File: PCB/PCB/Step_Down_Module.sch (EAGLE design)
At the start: 4 parts, among them Q1 TPH2900ENH

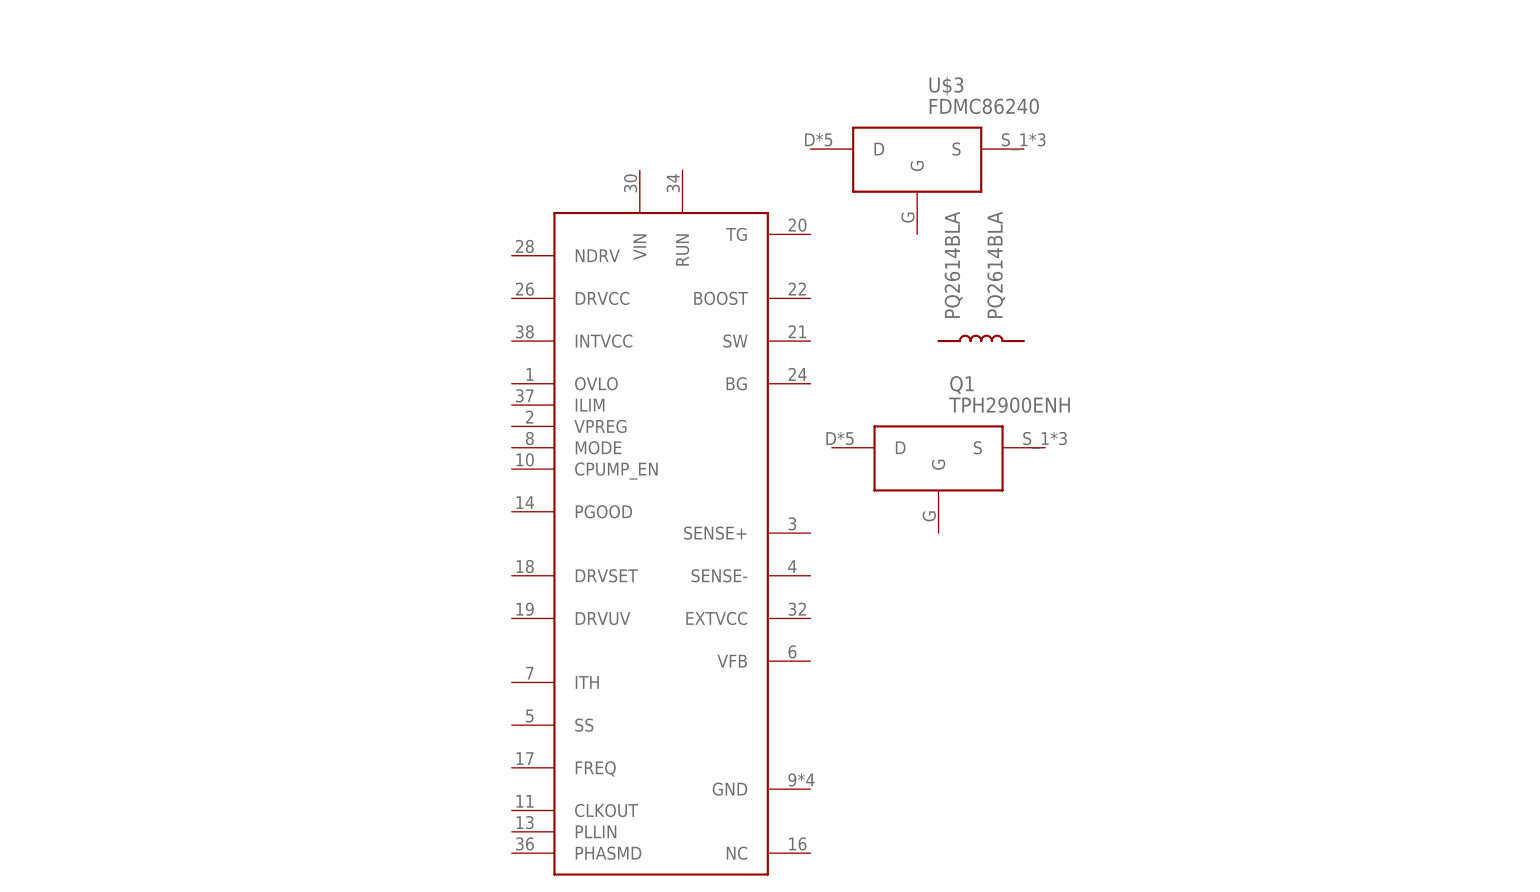
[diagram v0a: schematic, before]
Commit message: Working on schematic, slightly updated mosfets
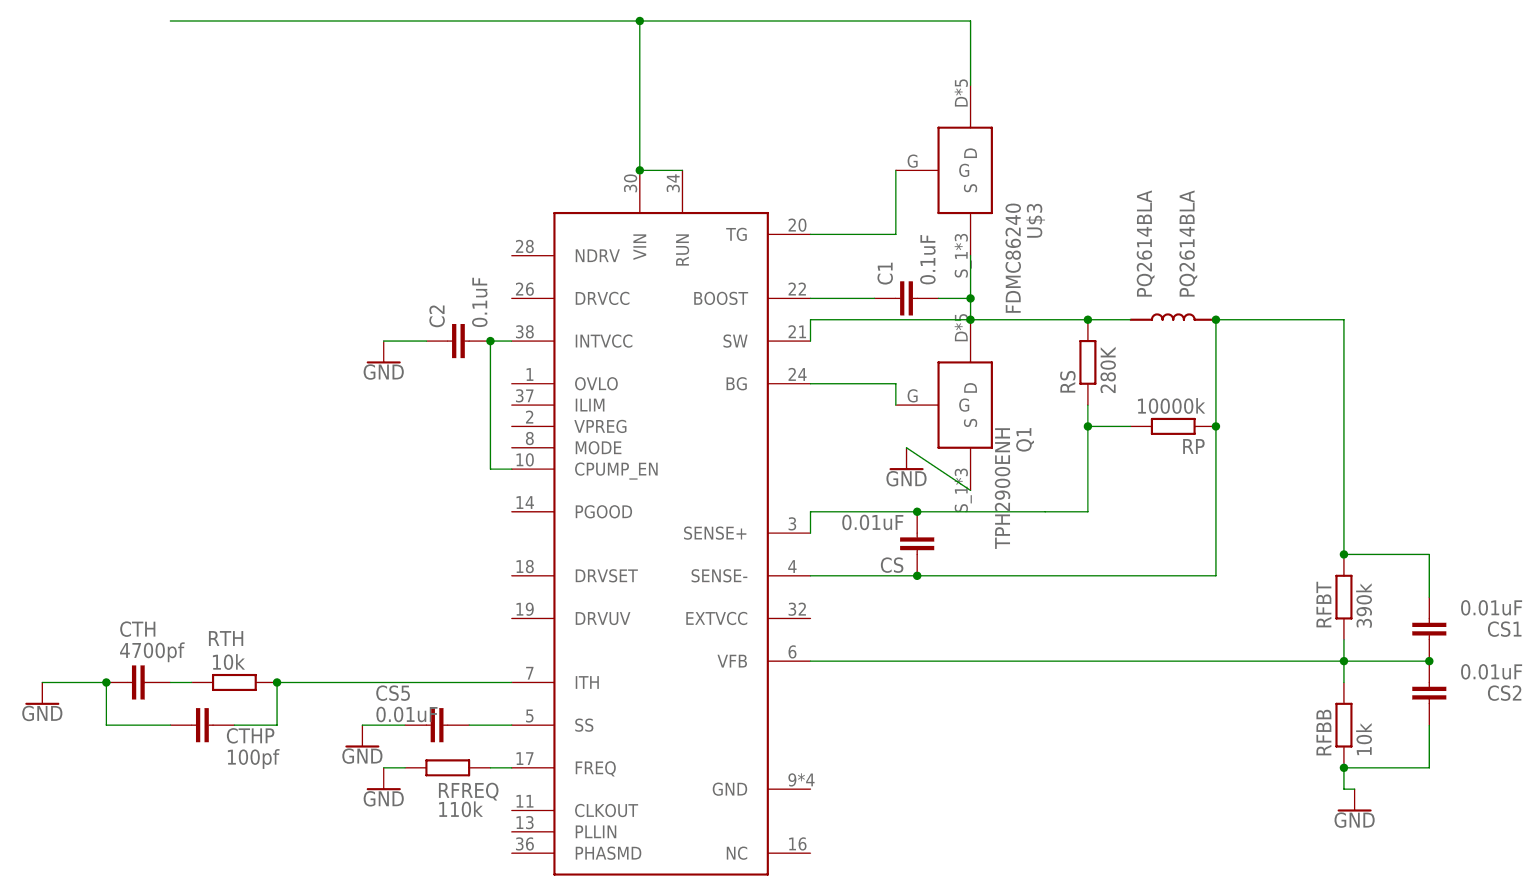
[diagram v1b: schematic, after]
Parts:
- added C1, C2: 0.1uF, rcl:C-EUC0805
- added CS, CS1, CS2, CS5: 0.01uF, rcl:C-EUC0805
- added CTH: 4700pf, rcl:C-EUC0805
- added CTHP: 100pf, rcl:C-EUC0805
- added RFBB, RTH: 10k, rcl:R-EU_R0805
- added RFBT: 390k, rcl:R-EU_R0805
- added RFREQ: 110k, rcl:R-EU_R0805
- added RP: 10000k, rcl:R-EU_R0805
- added RS: 280K, rcl:R-EU_R0805
- Q1: SPICEPREFIX (none) -> Q
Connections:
- new net GND: C2.1, CS2.1, CS5.2, CTH.2, CTHP.2, Q1.S, RFBB.1, RFREQ.1
- new net N$1: U$1.TG, U$3.G
- new net N$10: CTHP.1, RTH.1, U$1.ITH
- new net N$11: RFREQ.2, U$1.FREQ
- new net N$12: CTH.1, RTH.2
- new net N$13: C2.2, U$1.CPUMP_EN, U$1.INTVCC
- new net N$2: Q1.G, U$1.BG
- new net N$3: C1.2, Q1.D, RS.2, U$1.SW, U$2.P$1, U$3.S
- new net N$4: C1.1, U$1.BOOST
- new net N$5: CS.1, CS1.2, RFBT.2, RP.1, U$1.SENSE-, U$2.P$2
- new net N$6: CS.2, RP.2, RS.1, U$1.SENSE+
- new net N$7: CS5.1, U$1.SS
- new net N$8: CS1.1, CS2.2, RFBB.2, RFBT.1, U$1.VFB
- new net N$9: U$1.RUN, U$1.VIN, U$3.D
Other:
- moved on the sheet: Q1, U$3

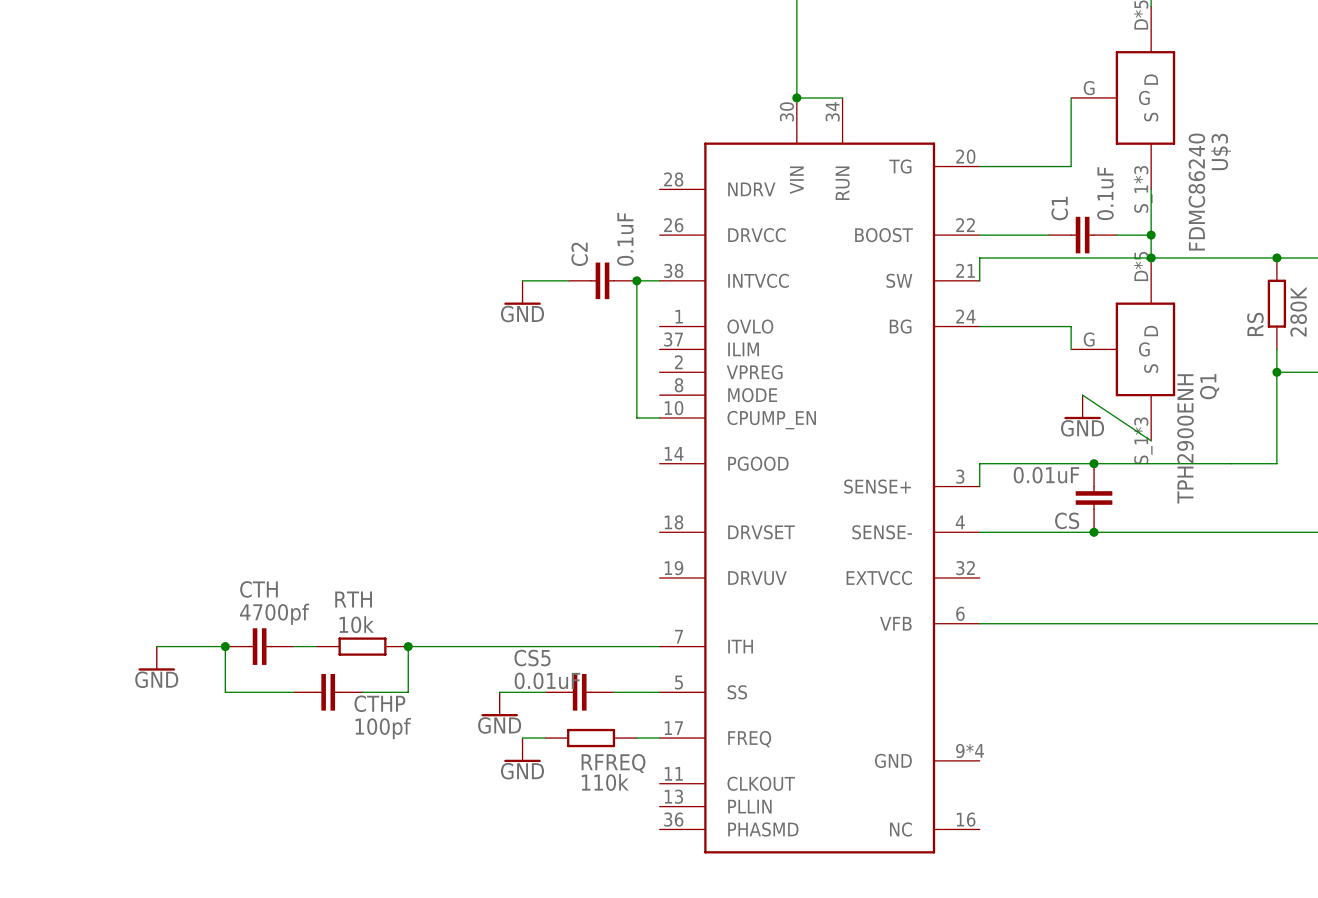
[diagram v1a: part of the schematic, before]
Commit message: Working on schematic - functions of other pins
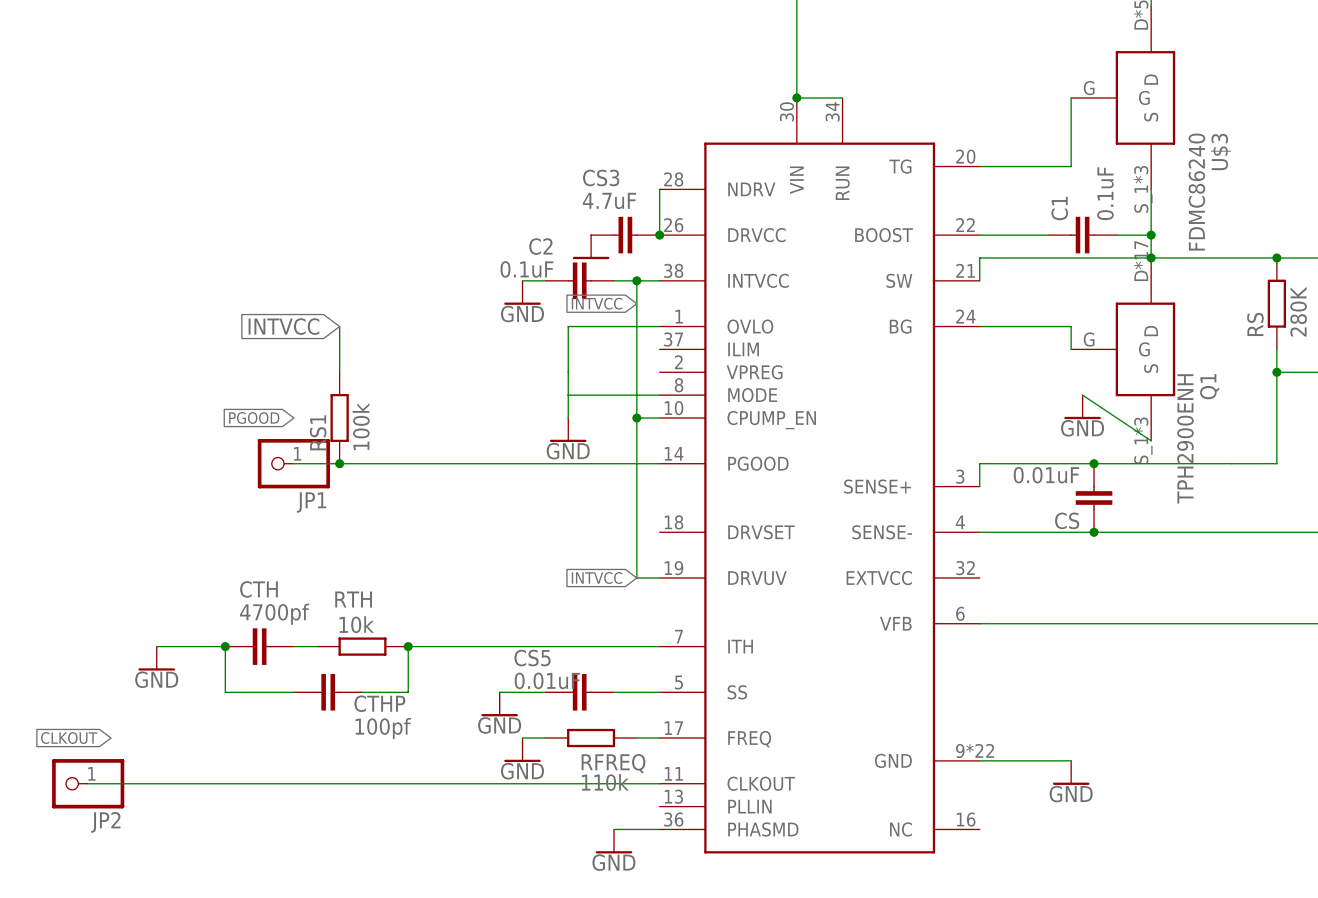
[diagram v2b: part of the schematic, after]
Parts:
- added CS3: 4.7uF, rcl:C-EUC0805
- added JP1, JP2: (no value), pinhead:PINHD-1X1
- added RS1: 100k, rcl:R-EU_R0805
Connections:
- removed net N$13: C2.2, U$1.CPUMP_EN, U$1.INTVCC
- new net CLKOUT: JP2.1, U$1.CLKOUT
- new net INTVCC: C2.2, RS1.2, U$1.CPUMP_EN, U$1.DRVUV, U$1.INTVCC
- new net N$14: CS3.1, U$1.DRVCC, U$1.NDRV
- new net PGOOD: JP1.1, RS1.1, U$1.PGOOD
- net GND: now also CS3.2, U$1.GND, U$1.MODE, U$1.OVLO, U$1.PHASMD
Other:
- moved on the sheet: C2, Q1
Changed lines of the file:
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@@
 <part name="C2" library="rcl" library_urn="urn:adsk.eagle:library:334" deviceset="C-EU" device="C0805" package3d_urn="urn:adsk.eagle:package:23617/2" value="0.1uF"/>
 <part name="GND6" library="SparkFun-PowerSymbols" library_urn="urn:adsk.eagle:library:530" deviceset="GND" device=""/>
+<part name="GND7" library="SparkFun-PowerSymbols" library_urn="urn:adsk.eagle:library:530" deviceset="GND" device=""/>
+<part name="GND8" library="SparkFun-PowerSymbols" library_urn="urn:adsk.eagle:library:530" deviceset="GND" device=""/>
+<part name="JP1" library="pinhead" library_urn="urn:adsk.eagle:library:325" deviceset="PINHD-1X1" device="" package3d_urn="urn:adsk.eagle:package:22485/2"/>
+<part name="RS1" library="rcl" library_urn="urn:adsk.eagle:library:334" deviceset="R-EU_" device="R0805" package3d_urn="urn:adsk.eagle:package:23553/2" value="100k"/>
+<part name="JP2" library="pinhead" library_urn="urn:adsk.eagle:library:325" deviceset="PINHD-1X1" device="" package3d_urn="urn:adsk.eagle:package:22485/2"/>
+<part name="GND9" library="SparkFun-PowerSymbols" library_urn="urn:adsk.eagle:library:530" deviceset="GND" device=""/>
+<part name="CS3" library="rcl" library_urn="urn:adsk.eagle:library:334" deviceset="C-EU" device="C0805" package3d_urn="urn:adsk.eagle:package:23617/2" value="4.7uF"/>
+<part name="GND10" library="SparkFun-PowerSymbols" library_urn="urn:adsk.eagle:library:530" deviceset="GND" device=""/>
 </parts>
 <sheets>
@@
 </instance>
 <instance part="GND5" gate="1" x="-12.7" y="17.78"/>
-<instance part="C2" gate="G$1" x="-5.08" y="71.12" rot="R90"/>
+<instance part="C2" gate="G$1" x="-7.62" y="71.12" smashed="yes" rot="R90">
+<attribute name="NAME" x="-9.144" y="75.819" size="1.778" layer="95" rot="R180"/>
+<attribute name="VALUE" x="-9.144" y="73.279" size="1.778" layer="96" rot="R180"/>
+</instance>
 <instance part="GND6" gate="1" x="-12.7" y="68.58"/>
+<instance part="GND7" gate="1" x="-7.62" y="53.34"/>
+<instance part="GND8" gate="1" x="48.26" y="15.24"/>
+<instance part="JP1" gate="G$1" x="-40.64" y="50.8" rot="R180"/>
+<instance part="RS1" gate="G$1" x="-33.02" y="55.88" rot="R90"/>
+<instance part="JP2" gate="G$1" x="-63.5" y="15.24" rot="R180"/>
+<instance part="GND9" gate="1" x="-2.54" y="7.62"/>
+<instance part="CS3" gate="G$1" x="0" y="76.2" smashed="yes" rot="R270">
+<attribute name="NAME" x="-6.096" y="81.661" size="1.778" layer="95"/>
+<attribute name="VALUE" x="-6.096" y="79.121" size="1.778" layer="96"/>
+</instance>
+<instance part="GND10" gate="1" x="-5.08" y="73.66" smashed="yes"/>
 </instances>
 <busses>
@@
 <pinref part="GND6" gate="1" pin="GND"/>
 <pinref part="C2" gate="G$1" pin="1"/>
-<wire x1="-12.7" y1="71.12" x2="-7.62" y2="71.12" width="0.1524" layer="91"/>
+<wire x1="-12.7" y1="71.12" x2="-10.16" y2="71.12" width="0.1524" layer="91"/>
+</segment>
+<segment>
+<pinref part="GND7" gate="1" pin="GND"/>
+<pinref part="U$1" gate="G$1" pin="OVLO"/>
+<wire x1="-7.62" y1="55.88" x2="-7.62" y2="58.42" width="0.1524" layer="91"/>
+<wire x1="-7.62" y1="60.96" x2="-7.62" y2="66.04" width="0.1524" layer="91"/>
+<wire x1="-7.62" y1="66.04" x2="2.54" y2="66.04" width="0.1524" layer="91"/>
+<pinref part="U$1" gate="G$1" pin="MODE"/>
+<wire x1="-7.62" y1="60.96" x2="-7.62" y2="58.42" width="0.1524" layer="91"/>
+<wire x1="-7.62" y1="58.42" x2="2.54" y2="58.42" width="0.1524" layer="91"/>
+</segment>
+<segment>
+<pinref part="U$1" gate="G$1" pin="GND"/>
+<pinref part="GND8" gate="1" pin="GND"/>
+<wire x1="38.1" y1="17.78" x2="48.26" y2="17.78" width="0.1524" layer="91"/>
+</segment>
+<segment>
+<pinref part="GND9" gate="1" pin="GND"/>
+<pinref part="U$1" gate="G$1" pin="PHASMD"/>
+<wire x1="-2.54" y1="10.16" x2="2.54" y2="10.16" width="0.1524" layer="91"/>
+</segment>
+<segment>
+<pinref part="CS3" gate="G$1" pin="2"/>
+<pinref part="GND10" gate="1" pin="GND"/>
 </segment>
 </net>
@@
 </segment>
 </net>
-<net name="N$13" class="0">
+<net name="INTVCC" class="0">
 <segment>
 <pinref part="C2" gate="G$1" pin="2"/>
 <pinref part="U$1" gate="G$1" pin="INTVCC"/>
+<wire x1="-2.54" y1="71.12" x2="0" y2="71.12" width="0.1524" layer="91"/>
 <wire x1="0" y1="71.12" x2="2.54" y2="71.12" width="0.1524" layer="91"/>
-<wire x1="0" y1="71.12" x2="0" y2="55.88" width="0.1524" layer="91"/>
-<junction x="0" y="71.12"/>
 <pinref part="U$1" gate="G$1" pin="CPUMP_EN"/>
 <wire x1="0" y1="55.88" x2="2.54" y2="55.88" width="0.1524" layer="91"/>
-</segment>
-</net>
+<label x="0" y="68.58" size="1.27" layer="95" rot="R180" xref="yes"/>
+<pinref part="U$1" gate="G$1" pin="DRVUV"/>
+<wire x1="2.54" y1="38.1" x2="0" y2="38.1" width="0.1524" layer="91"/>
+<wire x1="0" y1="38.1" x2="0" y2="55.88" width="0.1524" layer="91"/>
+<junction x="0" y="55.88"/>
+<label x="0" y="38.1" size="1.27" layer="95" rot="R180" xref="yes"/>
+<wire x1="0" y1="55.88" x2="0" y2="71.12" width="0.1524" layer="91"/>
+<junction x="0" y="71.12"/>
+</segment>
+<segment>
+<pinref part="RS1" gate="G$1" pin="2"/>
+<wire x1="-33.02" y1="60.96" x2="-33.02" y2="66.04" width="0.1524" layer="91"/>
+<label x="-33.02" y="66.04" size="1.778" layer="95" rot="R180" xref="yes"/>
+</segment>
+</net>
+<net name="PGOOD" class="0">
+<segment>
+<pinref part="U$1" gate="G$1" pin="PGOOD"/>
+<pinref part="JP1" gate="G$1" pin="1"/>
+<wire x1="2.54" y1="50.8" x2="-33.02" y2="50.8" width="0.1524" layer="91"/>
+<pinref part="RS1" gate="G$1" pin="1"/>
+<wire x1="-33.02" y1="50.8" x2="-38.1" y2="50.8" width="0.1524" layer="91"/>
+<junction x="-33.02" y="50.8"/>
+<label x="-38.1" y="55.88" size="1.27" layer="95" rot="R180" xref="yes"/>
+</segment>
+</net>
+<net name="CLKOUT" class="0">
+<segment>
+<pinref part="U$1" gate="G$1" pin="CLKOUT"/>
+<wire x1="2.54" y1="15.24" x2="-60.96" y2="15.24" width="0.1524" layer="91"/>
+<pinref part="JP2" gate="G$1" pin="1"/>
+<label x="-58.42" y="20.32" size="1.27" layer="95" rot="R180" xref="yes"/>
+</segment>
+</net>
+<net name="N$14" class="0">
+<segment>
+<pinref part="U$1" gate="G$1" pin="NDRV"/>
+<pinref part="U$1" gate="G$1" pin="DRVCC"/>
+<wire x1="2.54" y1="81.28" x2="2.54" y2="76.2" width="0.1524" layer="91"/>
+<pinref part="CS3" gate="G$1" pin="1"/>
+<junction x="2.54" y="76.2"/>
+</segment>
+</net>
